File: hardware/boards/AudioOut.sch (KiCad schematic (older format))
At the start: 9 parts, among them J4 AudioJack3_SwitchTR

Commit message: pcb w-i-p
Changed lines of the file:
@@
 $Descr A4 11693 8268
 encoding utf-8
-Sheet 3 8
+Sheet 2 8
 Title ""
 Date ""
@@
 AR Path="/5F0E4EB0/5F0C0CCE" Ref="C69"  Part="1"
 AR Path="/5F0EA26D/5F0C0CCE" Ref="C53"  Part="1"
-F 0 "C69" H 3115 2946 50  0000 L CNN
+F 0 "C45" H 3115 2946 50  0000 L CNN
 F 1 "4.7u" H 3115 2855 50  0000 L CNN
 F 2 "Capacitor_SMD:C_0805_2012Metric" H 3038 2750 50  0001 C CNN
@@
 AR Path="/5F0E4EB0/5F0C0D6D" Ref="C70"  Part="1"
 AR Path="/5F0EA26D/5F0C0D6D" Ref="C54"  Part="1"
-F 0 "C70" H 3115 4346 50  0000 L CNN
+F 0 "C46" H 3115 4346 50  0000 L CNN
 F 1 "4.7u" H 3115 4255 50  0000 L CNN
 F 2 "Capacitor_SMD:C_0805_2012Metric" H 3038 4150 50  0001 C CNN
@@
 AR Path="/5F0E4EB0/5F0C13C6" Ref="R34"  Part="1"
 AR Path="/5F0EA26D/5F0C13C6" Ref="R18"  Part="1"
-F 0 "R34" V 3643 2900 50  0000 C CNN
+F 0 "R10" V 3643 2900 50  0000 C CNN
 F 1 "560" V 3734 2900 50  0000 C CNN
 F 2 "Resistor_SMD:R_0805_2012Metric" V 3780 2900 50  0001 C CNN
@@
 AR Path="/5F0E4EB0/5F0C1FD3" Ref="R35"  Part="1"
 AR Path="/5F0EA26D/5F0C1FD3" Ref="R19"  Part="1"
-F 0 "R35" V 3643 4300 50  0000 C CNN
+F 0 "R11" V 3643 4300 50  0000 C CNN
 F 1 "560" V 3734 4300 50  0000 C CNN
 F 2 "Resistor_SMD:R_0805_2012Metric" V 3780 4300 50  0001 C CNN
@@
 AR Path="/5F0E4EB0/5F0C25D6" Ref="R33"  Part="1"
 AR Path="/5F0EA26D/5F0C25D6" Ref="R17"  Part="1"
-F 0 "R33" H 3330 4704 50  0000 R CNN
+F 0 "R9" H 3330 4704 50  0000 R CNN
 F 1 "10k" H 3330 4795 50  0000 R CNN
 F 2 "Resistor_SMD:R_0805_2012Metric" V 3330 4750 50  0001 C CNN
@@
 AR Path="/5F0E4EB0/5F0C364C" Ref="R32"  Part="1"
 AR Path="/5F0EA26D/5F0C364C" Ref="R16"  Part="1"
-F 0 "R32" H 3280 3304 50  0000 R CNN
+F 0 "R8" H 3280 3304 50  0000 R CNN
 F 1 "10k" H 3280 3395 50  0000 R CNN
 F 2 "Resistor_SMD:R_0805_2012Metric" V 3280 3350 50  0001 C CNN
@@
 AR Path="/5F0E4EB0/5F0C409A" Ref="C72"  Part="1"
 AR Path="/5F0EA26D/5F0C409A" Ref="C56"  Part="1"
-F 0 "C72" H 5115 4496 50  0000 L CNN
+F 0 "C48" H 5115 4496 50  0000 L CNN
 F 1 "2700p" H 5115 4405 50  0000 L CNN
 F 2 "Capacitor_SMD:C_0805_2012Metric" H 5038 4300 50  0001 C CNN
@@
 AR Path="/5F0E4EB0/5F0C470A" Ref="C71"  Part="1"
 AR Path="/5F0EA26D/5F0C470A" Ref="C55"  Part="1"
-F 0 "C71" H 5115 3446 50  0000 L CNN
+F 0 "C47" H 5115 3446 50  0000 L CNN
 F 1 "2700p" H 5115 3355 50  0000 L CNN
 F 2 "Capacitor_SMD:C_0805_2012Metric" H 5038 3250 50  0001 C CNN
@@
 AR Path="/5F0E4EB0/5F0C56B0" Ref="J10"  Part="1"
 AR Path="/5F0EA26D/5F0C56B0" Ref="J6"  Part="1"
-F 0 "J10" H 6270 2925 50  0000 R CNN
+F 0 "J4" H 6270 2925 50  0000 R CNN
 F 1 "AudioJack3_SwitchTR" H 6270 2834 50  0000 R CNN
 F 2 "footprints:ACJS-MV5" H 6550 3000 50  0001 C CNN

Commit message: wip
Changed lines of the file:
@@
 AR Path="/5F0E4EB0/5F0C0CCE" Ref="C69"  Part="1"
 AR Path="/5F0EA26D/5F0C0CCE" Ref="C53"  Part="1"
-F 0 "C45" H 3115 2946 50  0000 L CNN
+F 0 "C69" H 3115 2946 50  0000 L CNN
 F 1 "4.7u" H 3115 2855 50  0000 L CNN
 F 2 "Capacitor_SMD:C_0805_2012Metric" H 3038 2750 50  0001 C CNN
@@
 AR Path="/5F0E4EB0/5F0C0D6D" Ref="C70"  Part="1"
 AR Path="/5F0EA26D/5F0C0D6D" Ref="C54"  Part="1"
-F 0 "C46" H 3115 4346 50  0000 L CNN
+F 0 "C70" H 3115 4346 50  0000 L CNN
 F 1 "4.7u" H 3115 4255 50  0000 L CNN
 F 2 "Capacitor_SMD:C_0805_2012Metric" H 3038 4150 50  0001 C CNN
@@
 AR Path="/5F0E4EB0/5F0C13C6" Ref="R34"  Part="1"
 AR Path="/5F0EA26D/5F0C13C6" Ref="R18"  Part="1"
-F 0 "R10" V 3643 2900 50  0000 C CNN
+F 0 "R34" V 3643 2900 50  0000 C CNN
 F 1 "560" V 3734 2900 50  0000 C CNN
 F 2 "Resistor_SMD:R_0805_2012Metric" V 3780 2900 50  0001 C CNN
@@
 AR Path="/5F0E4EB0/5F0C1FD3" Ref="R35"  Part="1"
 AR Path="/5F0EA26D/5F0C1FD3" Ref="R19"  Part="1"
-F 0 "R11" V 3643 4300 50  0000 C CNN
+F 0 "R35" V 3643 4300 50  0000 C CNN
 F 1 "560" V 3734 4300 50  0000 C CNN
 F 2 "Resistor_SMD:R_0805_2012Metric" V 3780 4300 50  0001 C CNN
@@
 AR Path="/5F0E4EB0/5F0C25D6" Ref="R33"  Part="1"
 AR Path="/5F0EA26D/5F0C25D6" Ref="R17"  Part="1"
-F 0 "R9" H 3330 4704 50  0000 R CNN
+F 0 "R33" H 3330 4704 50  0000 R CNN
 F 1 "10k" H 3330 4795 50  0000 R CNN
 F 2 "Resistor_SMD:R_0805_2012Metric" V 3330 4750 50  0001 C CNN
@@
 AR Path="/5F0E4EB0/5F0C364C" Ref="R32"  Part="1"
 AR Path="/5F0EA26D/5F0C364C" Ref="R16"  Part="1"
-F 0 "R8" H 3280 3304 50  0000 R CNN
+F 0 "R32" H 3280 3304 50  0000 R CNN
 F 1 "10k" H 3280 3395 50  0000 R CNN
 F 2 "Resistor_SMD:R_0805_2012Metric" V 3280 3350 50  0001 C CNN
@@
 AR Path="/5F0E4EB0/5F0C409A" Ref="C72"  Part="1"
 AR Path="/5F0EA26D/5F0C409A" Ref="C56"  Part="1"
-F 0 "C48" H 5115 4496 50  0000 L CNN
+F 0 "C72" H 5115 4496 50  0000 L CNN
 F 1 "2700p" H 5115 4405 50  0000 L CNN
 F 2 "Capacitor_SMD:C_0805_2012Metric" H 5038 4300 50  0001 C CNN
@@
 AR Path="/5F0E4EB0/5F0C470A" Ref="C71"  Part="1"
 AR Path="/5F0EA26D/5F0C470A" Ref="C55"  Part="1"
-F 0 "C47" H 5115 3446 50  0000 L CNN
+F 0 "C71" H 5115 3446 50  0000 L CNN
 F 1 "2700p" H 5115 3355 50  0000 L CNN
 F 2 "Capacitor_SMD:C_0805_2012Metric" H 5038 3250 50  0001 C CNN
@@
 AR Path="/5F0E4EB0/5F0C56B0" Ref="J10"  Part="1"
 AR Path="/5F0EA26D/5F0C56B0" Ref="J6"  Part="1"
-F 0 "J4" H 6270 2925 50  0000 R CNN
+F 0 "J10" H 6270 2925 50  0000 R CNN
 F 1 "AudioJack3_SwitchTR" H 6270 2834 50  0000 R CNN
 F 2 "footprints:ACJS-MV5" H 6550 3000 50  0001 C CNN

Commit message: placing imprvmts
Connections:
- net AGND: now also J4.S; no longer J4.RN, J4.T, J4.TN
- net at C47.2, R10.1: now also J4.T; no longer J4.S
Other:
- moved on the sheet: J4
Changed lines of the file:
@@
 AR Path="/5F0E4EB0/5F0C0CCE" Ref="C69"  Part="1"
 AR Path="/5F0EA26D/5F0C0CCE" Ref="C53"  Part="1"
-F 0 "C69" H 3115 2946 50  0000 L CNN
+F 0 "C45" H 3115 2946 50  0000 L CNN
 F 1 "4.7u" H 3115 2855 50  0000 L CNN
 F 2 "Capacitor_SMD:C_0805_2012Metric" H 3038 2750 50  0001 C CNN
@@
 AR Path="/5F0E4EB0/5F0C0D6D" Ref="C70"  Part="1"
 AR Path="/5F0EA26D/5F0C0D6D" Ref="C54"  Part="1"
-F 0 "C70" H 3115 4346 50  0000 L CNN
+F 0 "C46" H 3115 4346 50  0000 L CNN
 F 1 "4.7u" H 3115 4255 50  0000 L CNN
 F 2 "Capacitor_SMD:C_0805_2012Metric" H 3038 4150 50  0001 C CNN
@@
 AR Path="/5F0E4EB0/5F0C13C6" Ref="R34"  Part="1"
 AR Path="/5F0EA26D/5F0C13C6" Ref="R18"  Part="1"
-F 0 "R34" V 3643 2900 50  0000 C CNN
+F 0 "R10" V 3643 2900 50  0000 C CNN
 F 1 "560" V 3734 2900 50  0000 C CNN
 F 2 "Resistor_SMD:R_0805_2012Metric" V 3780 2900 50  0001 C CNN
@@
 AR Path="/5F0E4EB0/5F0C1FD3" Ref="R35"  Part="1"
 AR Path="/5F0EA26D/5F0C1FD3" Ref="R19"  Part="1"
-F 0 "R35" V 3643 4300 50  0000 C CNN
+F 0 "R11" V 3643 4300 50  0000 C CNN
 F 1 "560" V 3734 4300 50  0000 C CNN
 F 2 "Resistor_SMD:R_0805_2012Metric" V 3780 4300 50  0001 C CNN
@@
 AR Path="/5F0E4EB0/5F0C25D6" Ref="R33"  Part="1"
 AR Path="/5F0EA26D/5F0C25D6" Ref="R17"  Part="1"
-F 0 "R33" H 3330 4704 50  0000 R CNN
+F 0 "R9" H 3330 4704 50  0000 R CNN
 F 1 "10k" H 3330 4795 50  0000 R CNN
 F 2 "Resistor_SMD:R_0805_2012Metric" V 3330 4750 50  0001 C CNN
@@
 AR Path="/5F0E4EB0/5F0C364C" Ref="R32"  Part="1"
 AR Path="/5F0EA26D/5F0C364C" Ref="R16"  Part="1"
-F 0 "R32" H 3280 3304 50  0000 R CNN
+F 0 "R8" H 3280 3304 50  0000 R CNN
 F 1 "10k" H 3280 3395 50  0000 R CNN
 F 2 "Resistor_SMD:R_0805_2012Metric" V 3280 3350 50  0001 C CNN
@@
 AR Path="/5F0E4EB0/5F0C409A" Ref="C72"  Part="1"
 AR Path="/5F0EA26D/5F0C409A" Ref="C56"  Part="1"
-F 0 "C72" H 5115 4496 50  0000 L CNN
+F 0 "C48" H 5115 4496 50  0000 L CNN
 F 1 "2700p" H 5115 4405 50  0000 L CNN
 F 2 "Capacitor_SMD:C_0805_2012Metric" H 5038 4300 50  0001 C CNN
@@
 AR Path="/5F0E4EB0/5F0C470A" Ref="C71"  Part="1"
 AR Path="/5F0EA26D/5F0C470A" Ref="C55"  Part="1"
-F 0 "C71" H 5115 3446 50  0000 L CNN
+F 0 "C47" H 5115 3446 50  0000 L CNN
 F 1 "2700p" H 5115 3355 50  0000 L CNN
 F 2 "Capacitor_SMD:C_0805_2012Metric" H 5038 3250 50  0001 C CNN
@@
 Wire Wire Line
 	5000 4900 5000 4600
-$Comp
-L Connector:AudioJack3_SwitchTR J4
-U 1 1 5F0C56B0
-P 6550 3000
-AR Path="/5F0BA363/5F0C56B0" Ref="J4"  Part="1"
-AR Path="/5F0DFE5E/5F0C56B0" Ref="J5"  Part="1"
-AR Path="/5F0E4EB0/5F0C56B0" Ref="J10"  Part="1"
-AR Path="/5F0EA26D/5F0C56B0" Ref="J6"  Part="1"
-F 0 "J10" H 6270 2925 50  0000 R CNN
-F 1 "AudioJack3_SwitchTR" H 6270 2834 50  0000 R CNN
-F 2 "footprints:ACJS-MV5" H 6550 3000 50  0001 C CNN
-F 3 "~" H 6550 3000 50  0001 C CNN
-	1    6550 3000
-	-1   0    0    -1
-$EndComp
-Wire Wire Line
-	6350 2900 5000 2900
-Connection ~ 5000 2900
-Wire Wire Line
-	6350 3000 5650 3000
-Wire Wire Line
-	5650 3000 5650 4300
 Wire Wire Line
 	5650 4300 5000 4300
 Connection ~ 5000 4300
-Wire Wire Line
-	6350 3100 6000 3100
-Wire Wire Line
-	6000 3100 6000 3200
-Wire Wire Line
-	6000 3300 6350 3300
-Wire Wire Line
-	6350 3200 6000 3200
-Connection ~ 6000 3200
-Wire Wire Line
-	6000 3200 6000 3300
 Text HLabel 2500 2900 0    50   Input ~ 0
 LEFT
@@
 	2450 3550 3350 3550
 Connection ~ 3350 3550
-Text Label 6000 3300 2    50   ~ 0
-AGND
 Text Label 5000 3550 0    50   ~ 0
 AGND
 Text Label 5000 4900 0    50   ~ 0
 AGND
+Connection ~ 5000 2900
+$Comp
+L Connector:AudioJack3_SwitchTR J4
+U 1 1 5F0C56B0
+P 6600 3100
+AR Path="/5F0BA363/5F0C56B0" Ref="J4"  Part="1"
+AR Path="/5F0DFE5E/5F0C56B0" Ref="J5"  Part="1"
+AR Path="/5F0E4EB0/5F0C56B0" Ref="J10"  Part="1"
+AR Path="/5F0EA26D/5F0C56B0" Ref="J6"  Part="1"
+F 0 "J4" H 6320 3025 50  0000 R CNN
+F 1 "AudioJack3_SwitchTR" H 6320 2934 50  0000 R CNN
+F 2 "footprints:ACJS-MV5" H 6600 3100 50  0001 C CNN
+F 3 "~" H 6600 3100 50  0001 C CNN
+	1    6600 3100
+	-1   0    0    1
+$EndComp
+Text Label 6050 3200 2    50   ~ 0
+AGND
+Wire Wire Line
+	6400 3200 6050 3200
+Wire Wire Line
+	6400 3100 5650 3100
+Wire Wire Line
+	5650 3100 5650 4300
+Wire Wire Line
+	5000 2900 6400 2900
 $EndSCHEMATC

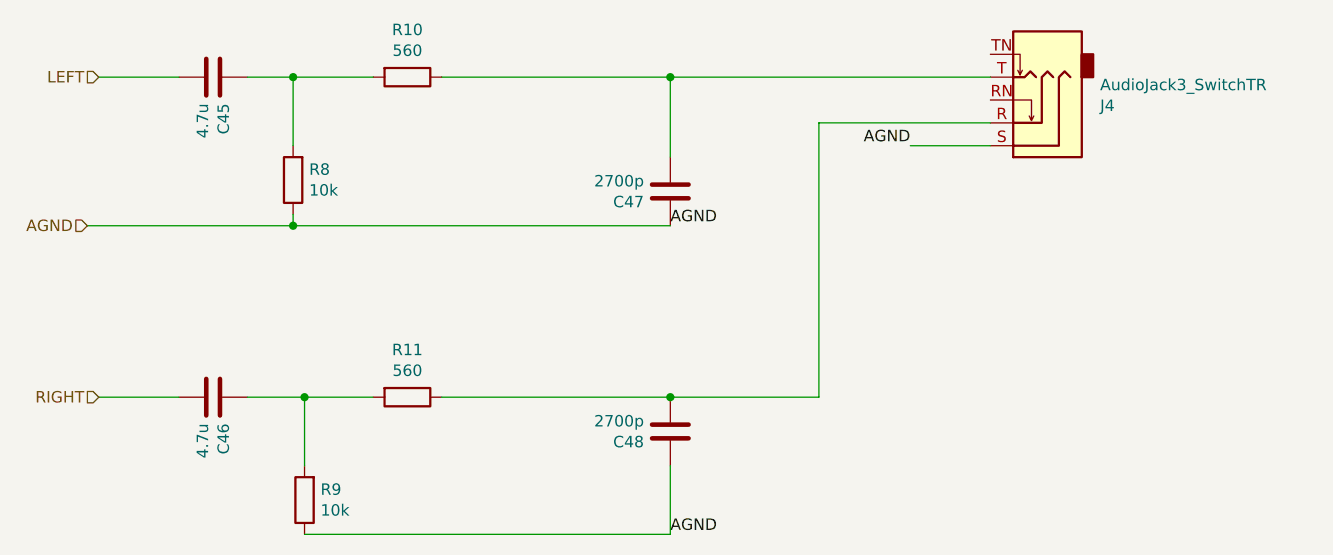
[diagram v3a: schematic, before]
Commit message: silkscreen, corrections
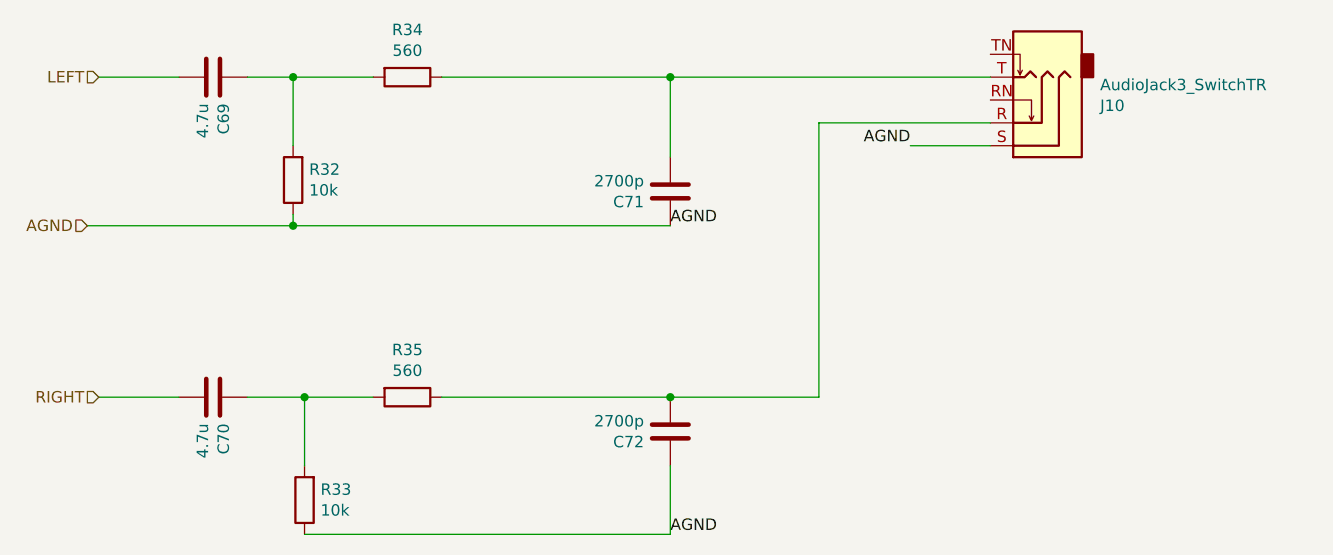
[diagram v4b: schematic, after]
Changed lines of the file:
@@
 AR Path="/5F0E4EB0/5F0C0CCE" Ref="C69"  Part="1"
 AR Path="/5F0EA26D/5F0C0CCE" Ref="C53"  Part="1"
-F 0 "C45" H 3115 2946 50  0000 L CNN
+F 0 "C69" H 3115 2946 50  0000 L CNN
 F 1 "4.7u" H 3115 2855 50  0000 L CNN
 F 2 "Capacitor_SMD:C_0805_2012Metric" H 3038 2750 50  0001 C CNN
@@
 AR Path="/5F0E4EB0/5F0C0D6D" Ref="C70"  Part="1"
 AR Path="/5F0EA26D/5F0C0D6D" Ref="C54"  Part="1"
-F 0 "C46" H 3115 4346 50  0000 L CNN
+F 0 "C70" H 3115 4346 50  0000 L CNN
 F 1 "4.7u" H 3115 4255 50  0000 L CNN
 F 2 "Capacitor_SMD:C_0805_2012Metric" H 3038 4150 50  0001 C CNN
@@
 AR Path="/5F0E4EB0/5F0C13C6" Ref="R34"  Part="1"
 AR Path="/5F0EA26D/5F0C13C6" Ref="R18"  Part="1"
-F 0 "R10" V 3643 2900 50  0000 C CNN
+F 0 "R34" V 3643 2900 50  0000 C CNN
 F 1 "560" V 3734 2900 50  0000 C CNN
 F 2 "Resistor_SMD:R_0805_2012Metric" V 3780 2900 50  0001 C CNN
@@
 AR Path="/5F0E4EB0/5F0C1FD3" Ref="R35"  Part="1"
 AR Path="/5F0EA26D/5F0C1FD3" Ref="R19"  Part="1"
-F 0 "R11" V 3643 4300 50  0000 C CNN
+F 0 "R35" V 3643 4300 50  0000 C CNN
 F 1 "560" V 3734 4300 50  0000 C CNN
 F 2 "Resistor_SMD:R_0805_2012Metric" V 3780 4300 50  0001 C CNN
@@
 AR Path="/5F0E4EB0/5F0C25D6" Ref="R33"  Part="1"
 AR Path="/5F0EA26D/5F0C25D6" Ref="R17"  Part="1"
-F 0 "R9" H 3330 4704 50  0000 R CNN
+F 0 "R33" H 3330 4704 50  0000 R CNN
 F 1 "10k" H 3330 4795 50  0000 R CNN
 F 2 "Resistor_SMD:R_0805_2012Metric" V 3330 4750 50  0001 C CNN
@@
 AR Path="/5F0E4EB0/5F0C364C" Ref="R32"  Part="1"
 AR Path="/5F0EA26D/5F0C364C" Ref="R16"  Part="1"
-F 0 "R8" H 3280 3304 50  0000 R CNN
+F 0 "R32" H 3280 3304 50  0000 R CNN
 F 1 "10k" H 3280 3395 50  0000 R CNN
 F 2 "Resistor_SMD:R_0805_2012Metric" V 3280 3350 50  0001 C CNN
@@
 AR Path="/5F0E4EB0/5F0C409A" Ref="C72"  Part="1"
 AR Path="/5F0EA26D/5F0C409A" Ref="C56"  Part="1"
-F 0 "C48" H 5115 4496 50  0000 L CNN
+F 0 "C72" H 5115 4496 50  0000 L CNN
 F 1 "2700p" H 5115 4405 50  0000 L CNN
 F 2 "Capacitor_SMD:C_0805_2012Metric" H 5038 4300 50  0001 C CNN
@@
 AR Path="/5F0E4EB0/5F0C470A" Ref="C71"  Part="1"
 AR Path="/5F0EA26D/5F0C470A" Ref="C55"  Part="1"
-F 0 "C47" H 5115 3446 50  0000 L CNN
+F 0 "C71" H 5115 3446 50  0000 L CNN
 F 1 "2700p" H 5115 3355 50  0000 L CNN
 F 2 "Capacitor_SMD:C_0805_2012Metric" H 5038 3250 50  0001 C CNN
@@
 AR Path="/5F0E4EB0/5F0C56B0" Ref="J10"  Part="1"
 AR Path="/5F0EA26D/5F0C56B0" Ref="J6"  Part="1"
-F 0 "J4" H 6320 3025 50  0000 R CNN
+F 0 "J10" H 6320 3025 50  0000 R CNN
 F 1 "AudioJack3_SwitchTR" H 6320 2934 50  0000 R CNN
 F 2 "footprints:ACJS-MV5" H 6600 3100 50  0001 C CNN

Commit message: erc pass
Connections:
- no-connect marks 0 -> 2
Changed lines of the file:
@@
 AR Path="/5F0E4EB0/5F0C0CCE" Ref="C69"  Part="1"
 AR Path="/5F0EA26D/5F0C0CCE" Ref="C53"  Part="1"
-F 0 "C69" H 3115 2946 50  0000 L CNN
+F 0 "C45" H 3115 2946 50  0000 L CNN
 F 1 "4.7u" H 3115 2855 50  0000 L CNN
 F 2 "Capacitor_SMD:C_0805_2012Metric" H 3038 2750 50  0001 C CNN
@@
 AR Path="/5F0E4EB0/5F0C0D6D" Ref="C70"  Part="1"
 AR Path="/5F0EA26D/5F0C0D6D" Ref="C54"  Part="1"
-F 0 "C70" H 3115 4346 50  0000 L CNN
+F 0 "C46" H 3115 4346 50  0000 L CNN
 F 1 "4.7u" H 3115 4255 50  0000 L CNN
 F 2 "Capacitor_SMD:C_0805_2012Metric" H 3038 4150 50  0001 C CNN
@@
 AR Path="/5F0E4EB0/5F0C13C6" Ref="R34"  Part="1"
 AR Path="/5F0EA26D/5F0C13C6" Ref="R18"  Part="1"
-F 0 "R34" V 3643 2900 50  0000 C CNN
+F 0 "R10" V 3643 2900 50  0000 C CNN
 F 1 "560" V 3734 2900 50  0000 C CNN
 F 2 "Resistor_SMD:R_0805_2012Metric" V 3780 2900 50  0001 C CNN
@@
 AR Path="/5F0E4EB0/5F0C1FD3" Ref="R35"  Part="1"
 AR Path="/5F0EA26D/5F0C1FD3" Ref="R19"  Part="1"
-F 0 "R35" V 3643 4300 50  0000 C CNN
+F 0 "R11" V 3643 4300 50  0000 C CNN
 F 1 "560" V 3734 4300 50  0000 C CNN
 F 2 "Resistor_SMD:R_0805_2012Metric" V 3780 4300 50  0001 C CNN
@@
 AR Path="/5F0E4EB0/5F0C25D6" Ref="R33"  Part="1"
 AR Path="/5F0EA26D/5F0C25D6" Ref="R17"  Part="1"
-F 0 "R33" H 3330 4704 50  0000 R CNN
+F 0 "R9" H 3330 4704 50  0000 R CNN
 F 1 "10k" H 3330 4795 50  0000 R CNN
 F 2 "Resistor_SMD:R_0805_2012Metric" V 3330 4750 50  0001 C CNN
@@
 AR Path="/5F0E4EB0/5F0C364C" Ref="R32"  Part="1"
 AR Path="/5F0EA26D/5F0C364C" Ref="R16"  Part="1"
-F 0 "R32" H 3280 3304 50  0000 R CNN
+F 0 "R8" H 3280 3304 50  0000 R CNN
 F 1 "10k" H 3280 3395 50  0000 R CNN
 F 2 "Resistor_SMD:R_0805_2012Metric" V 3280 3350 50  0001 C CNN
@@
 AR Path="/5F0E4EB0/5F0C409A" Ref="C72"  Part="1"
 AR Path="/5F0EA26D/5F0C409A" Ref="C56"  Part="1"
-F 0 "C72" H 5115 4496 50  0000 L CNN
+F 0 "C48" H 5115 4496 50  0000 L CNN
 F 1 "2700p" H 5115 4405 50  0000 L CNN
 F 2 "Capacitor_SMD:C_0805_2012Metric" H 5038 4300 50  0001 C CNN
@@
 AR Path="/5F0E4EB0/5F0C470A" Ref="C71"  Part="1"
 AR Path="/5F0EA26D/5F0C470A" Ref="C55"  Part="1"
-F 0 "C71" H 5115 3446 50  0000 L CNN
+F 0 "C47" H 5115 3446 50  0000 L CNN
 F 1 "2700p" H 5115 3355 50  0000 L CNN
 F 2 "Capacitor_SMD:C_0805_2012Metric" H 5038 3250 50  0001 C CNN
@@
 AR Path="/5F0E4EB0/5F0C56B0" Ref="J10"  Part="1"
 AR Path="/5F0EA26D/5F0C56B0" Ref="J6"  Part="1"
-F 0 "J10" H 6320 3025 50  0000 R CNN
+F 0 "J4" H 6320 3025 50  0000 R CNN
 F 1 "AudioJack3_SwitchTR" H 6320 2934 50  0000 R CNN
 F 2 "footprints:ACJS-MV5" H 6600 3100 50  0001 C CNN
@@
 Wire Wire Line
 	5000 2900 6400 2900
+NoConn ~ 6400 3000
+NoConn ~ 6400 2800
 $EndSCHEMATC
